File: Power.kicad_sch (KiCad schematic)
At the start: 0 parts

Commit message: Power schematic
Updated the power schematic sheet.
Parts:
- added C1: 2200u, Capacitor_SMD:CP_Elec_10x10, symbol Device:C_Polarized
- added C2: 2200u, Capacitor_SMD:CP_Elec_16x17.5, symbol Device:C_Polarized
- added C3, C4: 2u2, Capacitor_SMD:CP_Elec_4x5.4, symbol Device:C_Polarized
- added D1: MDB6S, Package_SO:TSSOP-4_4.4x5mm_P4mm, symbol Diode_Bridge:MDB6S
- added J1, J2: Conn_01x01_Socket, Connector_Wire:SolderWire-2.5sqmm_1x01_D2.4mm_OD4.4mm, symbol Connector:Conn_01x01_Socket
- added TR1: TEZ10.0-D-2, Transformer_THT:Transformer_Breve_TEZ-44x52, symbol Transformer:TEZ10.0-D-2
- added U2: LM337_SOT223, Package_TO_SOT_SMD:SOT-223-3_TabPin2, symbol Regulator_Linear:LM337_SOT223
- added U3: LM317_SOT-223, Package_TO_SOT_SMD:SOT-223-3_TabPin2, symbol Regulator_Linear:LM317_SOT-223
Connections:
- new net: J1.1 (Pin_1), TR1.1
- new net: J2.1 (Pin_1), TR1.6

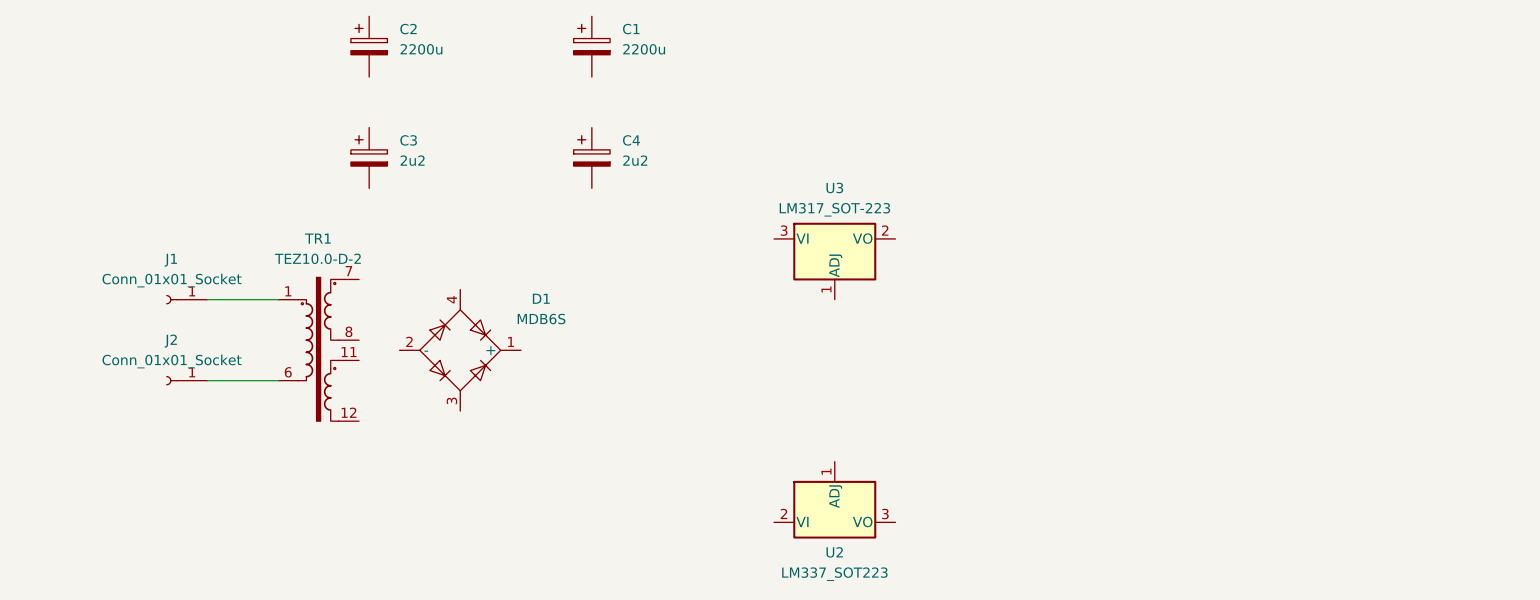
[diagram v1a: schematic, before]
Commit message: Power Supply
Added the power supply board.
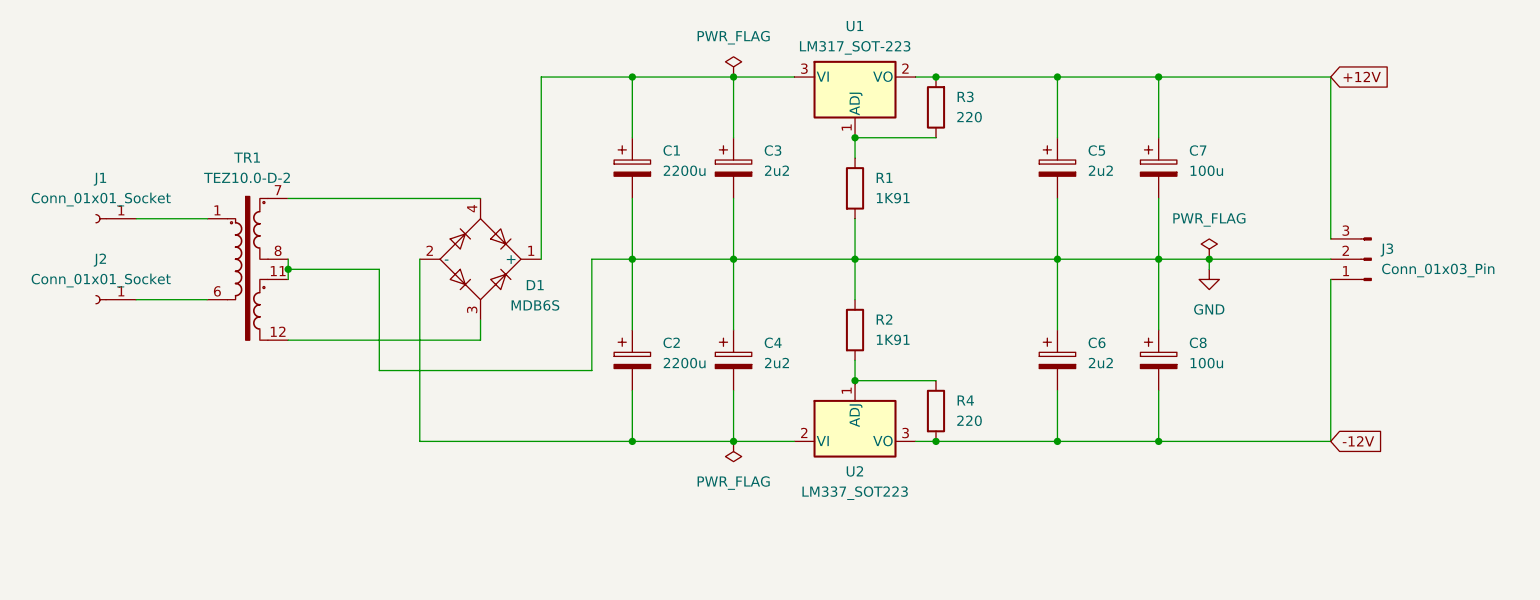
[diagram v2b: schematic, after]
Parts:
- added C5, C6: 2u2, Capacitor_SMD:CP_Elec_4x5.4, symbol Device:C_Polarized
- added C7, C8: 100u, Capacitor_SMD:CP_Elec_6.3x7.7, symbol Device:C_Polarized
- added J3: Conn_01x03_Pin, Connector_Molex:Molex_KK-254_AE-6410-03A_1x03_P2.54mm_Vertical, symbol Connector:Conn_01x03_Pin
- added R1, R2: 1K91, Resistor_SMD:R_0805_2012Metric_Pad1.20x1.40mm_HandSolder, symbol Device:R
- added R3, R4: 220, Resistor_SMD:R_0805_2012Metric_Pad1.20x1.40mm_HandSolder, symbol Device:R
- C1: footprint Capacitor_SMD:CP_Elec_10x10 -> Capacitor_SMD:CP_Elec_16x17.5
- D1: footprint Package_SO:TSSOP-4_4.4x5mm_P4mm -> Custom_Parts:TSSOP-4_4.4x5mm_P4mm
- renumbered U3 to U1
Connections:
- net at D1.1 (+): now also C1.1, C3.1, U1.3 (VI)
- net at D1.2 (-): now also C2.2, C4.2, U2.2 (VI)
- net at D1.3: now also TR1.12
- net at D1.4: now also TR1.7
- net at U1.1 (ADJ): now also R1.1, R3.1
- net +12V: now reaches U1.2 (VO)
- net +12V: now also C5.1, C7.1, J3.3 (Pin_3), R3.2
- net GND: now reaches C1.2
- net GND: now also C2.1, C3.2, C4.1, TR1.11, TR1.8, C5.2, C6.1, C7.2, C8.1, J3.2 (Pin_2), R1.2, R2.1
- net at U2.1 (ADJ): now also R2.2, R4.1
- net -12V: now reaches U2.3 (VO)
- net -12V: now also C6.2, C8.2, J3.1 (Pin_1), R4.2
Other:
- moved on the sheet: C1, C2, C3, C4, D1, J1, J2, TR1, U1, U2

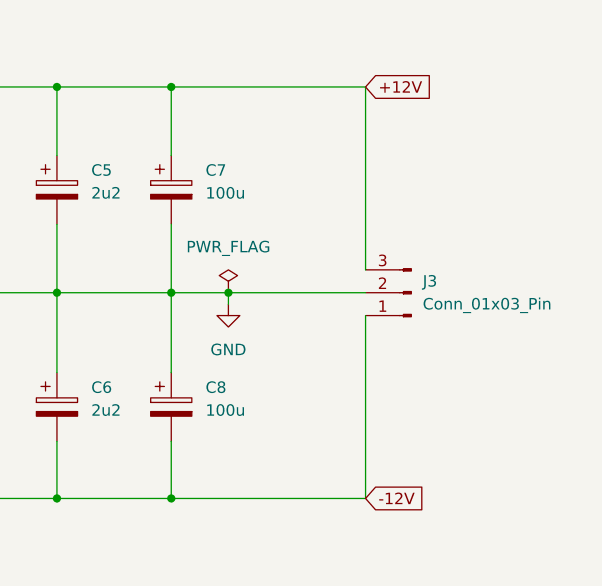
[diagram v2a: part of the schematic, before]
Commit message: Preamp Schematic
Added the preamplifier schematic.
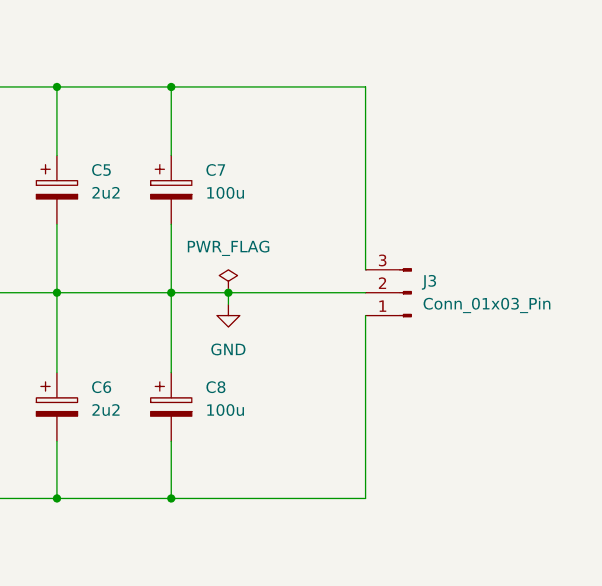
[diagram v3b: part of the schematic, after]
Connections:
- net +12V: no longer names the net of C5.1, C7.1, J3.3 (Pin_3), R3.2, U1.2 (VO)
- net -12V: no longer names the net of C6.2, C8.2, J3.1 (Pin_1), R4.2, U2.3 (VO)
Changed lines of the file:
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@@
-		)
-	)
-	(global_label "+12V"
-		(shape input)
-		(at 214.63 73.66 0)
-		(fields_autoplaced yes)
-		(effects
-			(font
-				(size 1.27 1.27)
-			)
-			(justify left)
-		)
-		(property "Intersheetrefs" "${INTERSHEET_REFS}"
-			(at 222.6952 73.66 0)
-			(effects
-				(font
-					(size 1.27 1.27)
-				)
-				(justify left)
-				(hide yes)
-			)
-		)
-	)
-	(global_label "-12V"
-		(shape input)
-		(at 214.63 119.38 0)
-		(fields_autoplaced yes)
-		(effects
-			(font
-				(size 1.27 1.27)
-			)
-			(justify left)
-		)
-		(property "Intersheetrefs" "${INTERSHEET_REFS}"
-			(at 222.6952 119.38 0)
-			(effects
-				(font
-					(size 1.27 1.27)
-				)
-				(justify left)
-				(hide yes)
-			)
 		)
 	)
